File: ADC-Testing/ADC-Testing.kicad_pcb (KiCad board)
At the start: 4 copper layers, 64.5 x 58 mm, 23 parts, among them SW1 SW_Push, U1 Adafruit_Feather_Generic, U2 MCP3561RT-E/ST, U3 DAC8311, U4 ADCS37041, U5 TC1016-3.3V

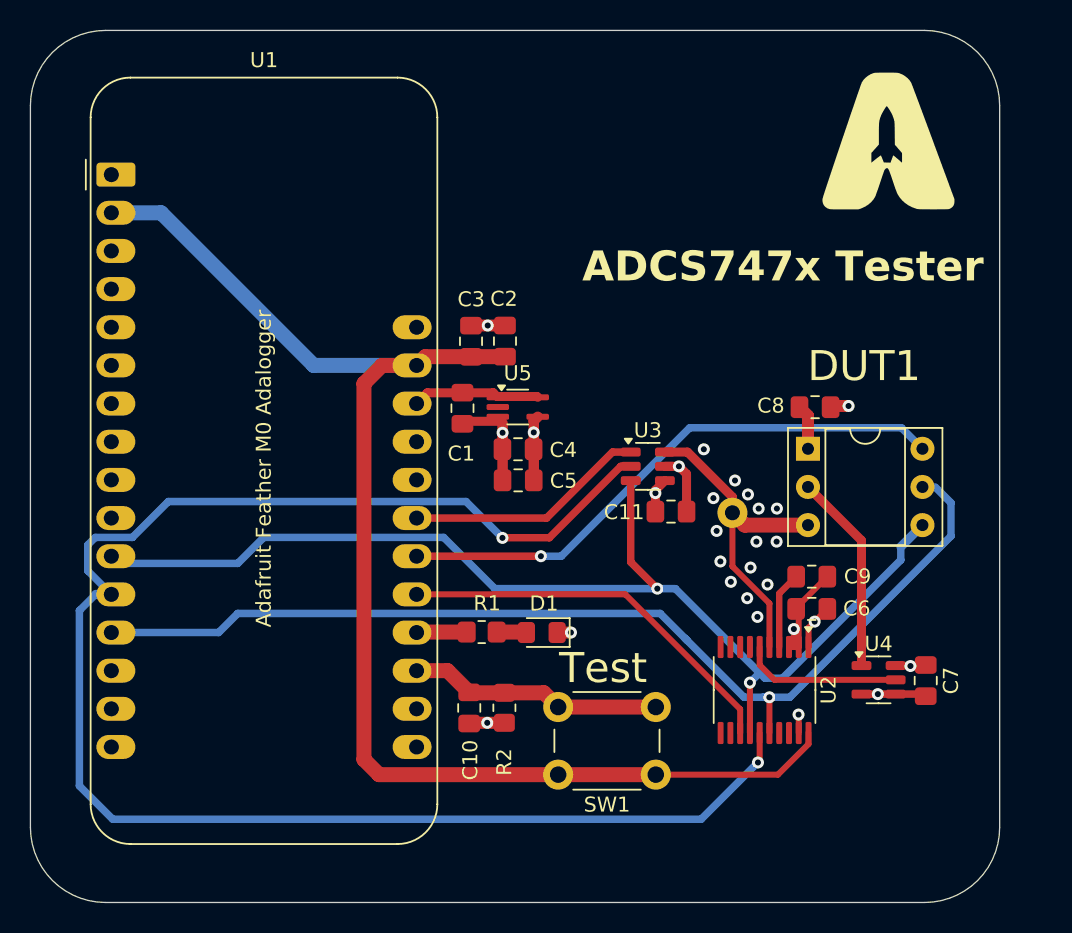
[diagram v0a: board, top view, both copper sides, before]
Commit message: adc testing move to v9
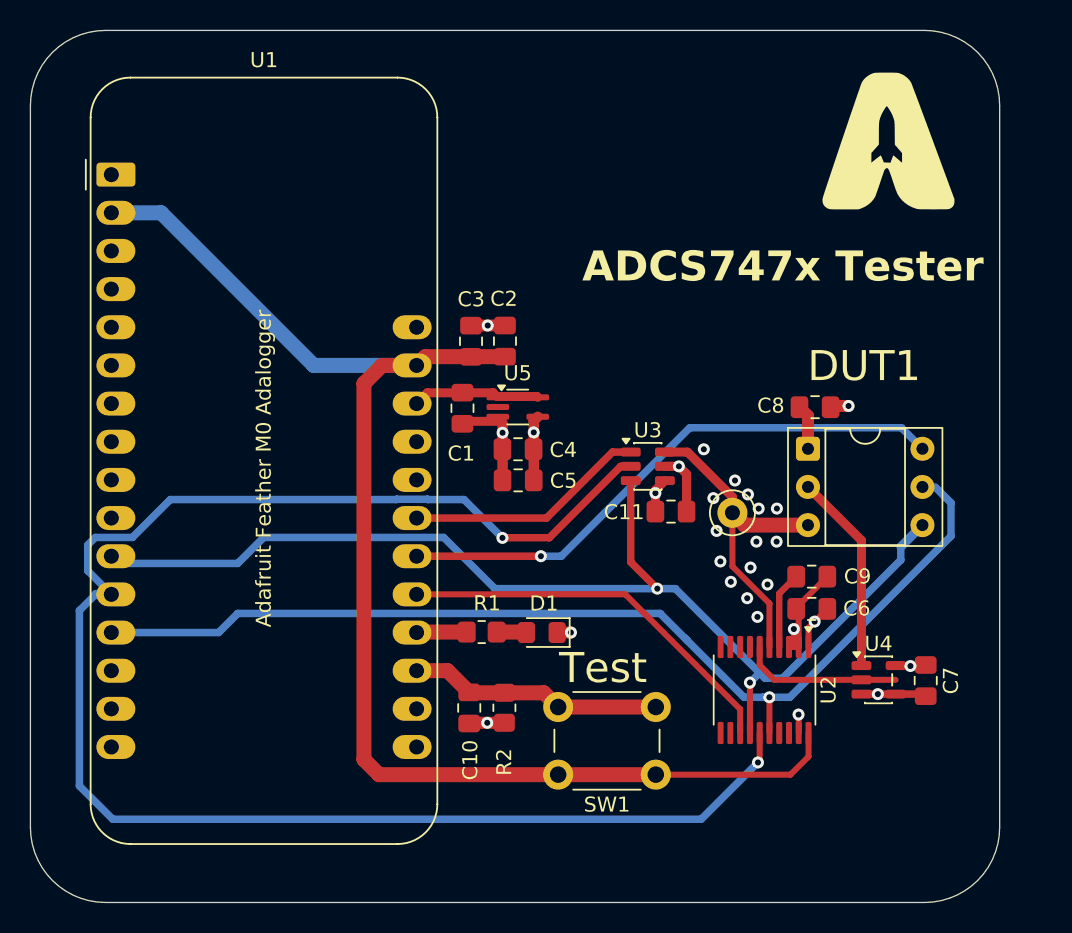
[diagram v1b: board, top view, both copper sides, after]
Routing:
- net VDDA: track 68.2 -> 66.7 mm
